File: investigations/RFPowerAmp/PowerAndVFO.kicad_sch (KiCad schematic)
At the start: 5 parts, among them J504 CONN_20

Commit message: Starting work on VFO
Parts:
- added Y601: ASTX-H11-25.000MHZ-T, ASTXH1124576MHZT, symbol ASTX-H11:ASTX-H11
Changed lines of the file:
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@@
     (effects (font (size 1.27 1.27)) (justify left top))
+  )
+  (symbol (lib_id "ASTX-H11:ASTX-H11") (at 39.37 43.18 0) (unit 1)
+    (in_bom yes) (on_board yes) (dnp no) (fields_autoplaced)
+    (property "Reference" "Y601" (at 59.69 35.56 0)
+      (effects (font (size 1.27 1.27)))
+    )
+    (property "Value" "ASTX-H11-25.000MHZ-T" (at 59.69 38.1 0)
+      (effects (font (size 1.27 1.27)))
+    )
+    (property "Footprint" "ASTXH1124576MHZT" (at 76.2 138.1 0)
+      (effects (font (size 1.27 1.27)) (justify left top) hide)
+    )
+    (property "Datasheet" "https://abracon.com/Oscillators/ASTX-H11.pdf" (at 76.2 238.1 0)
+      (effects (font (size 1.27 1.27)) (justify left top) hide)
+    )
+    (property "Height" "1.1" (at 76.2 438.1 0)
+      (effects (font (size 1.27 1.27)) (justify left top) hide)
+    )
+    (property "Manufacturer_Name" "ABRACON" (at 76.2 538.1 0)
+      (effects (font (size 1.27 1.27)) (justify left top) hide)
+    )
+    (property "Manufacturer_Part_Number" "ASTX-H11-##.###MHZ-T" (at 76.2 638.1 0)
+      (effects (font (size 1.27 1.27)) (justify left top) hide)
+    )
+    (property "Mouser Part Number" "815-ASTXH11" (at 76.2 738.1 0)
+      (effects (font (size 1.27 1.27)) (justify left top) hide)
+    )
+    (property "Mouser Price/Stock" "https://www.mouser.co.uk/ProductDetail/ABRACON/ASTX-H11-24000MHZ-T?qs=tfZGHB2PWd1qJqhLOR%252BN0w%3D%3D" (at 76.2 838.1 0)
+      (effects (font (size 1.27 1.27)) (justify left top) hide)
+    )
+    (property "Arrow Part Number" "ASTX-H11-##.###MHZ-T" (at 76.2 938.1 0)
+      (effects (font (size 1.27 1.27)) (justify left top) hide)
+    )
+    (property "Arrow Price/Stock" "https://www.arrow.com/en/products/astx-h11-24.000mhz-t/abracon" (at 76.2 1038.1 0)
+      (effects (font (size 1.27 1.27)) (justify left top) hide)
+    )
+    (pin "1")
+    (pin "2")
+    (pin "3")
+    (pin "4")
+    (instances
+      (project "RFPowerAmp"
+        (path "/4eeb911c-75f4-4119-b54f-fc9266b9abf0/204ca3ab-d207-410f-930a-76704dfa57fb"
+          (reference "Y601") (unit 1)
+        )
+      )
+    )
   )
   (symbol (lib_id "SparkFun-Connectors:CONN_20") (at 34.29 137.16 0) (mirror x) (unit 1)

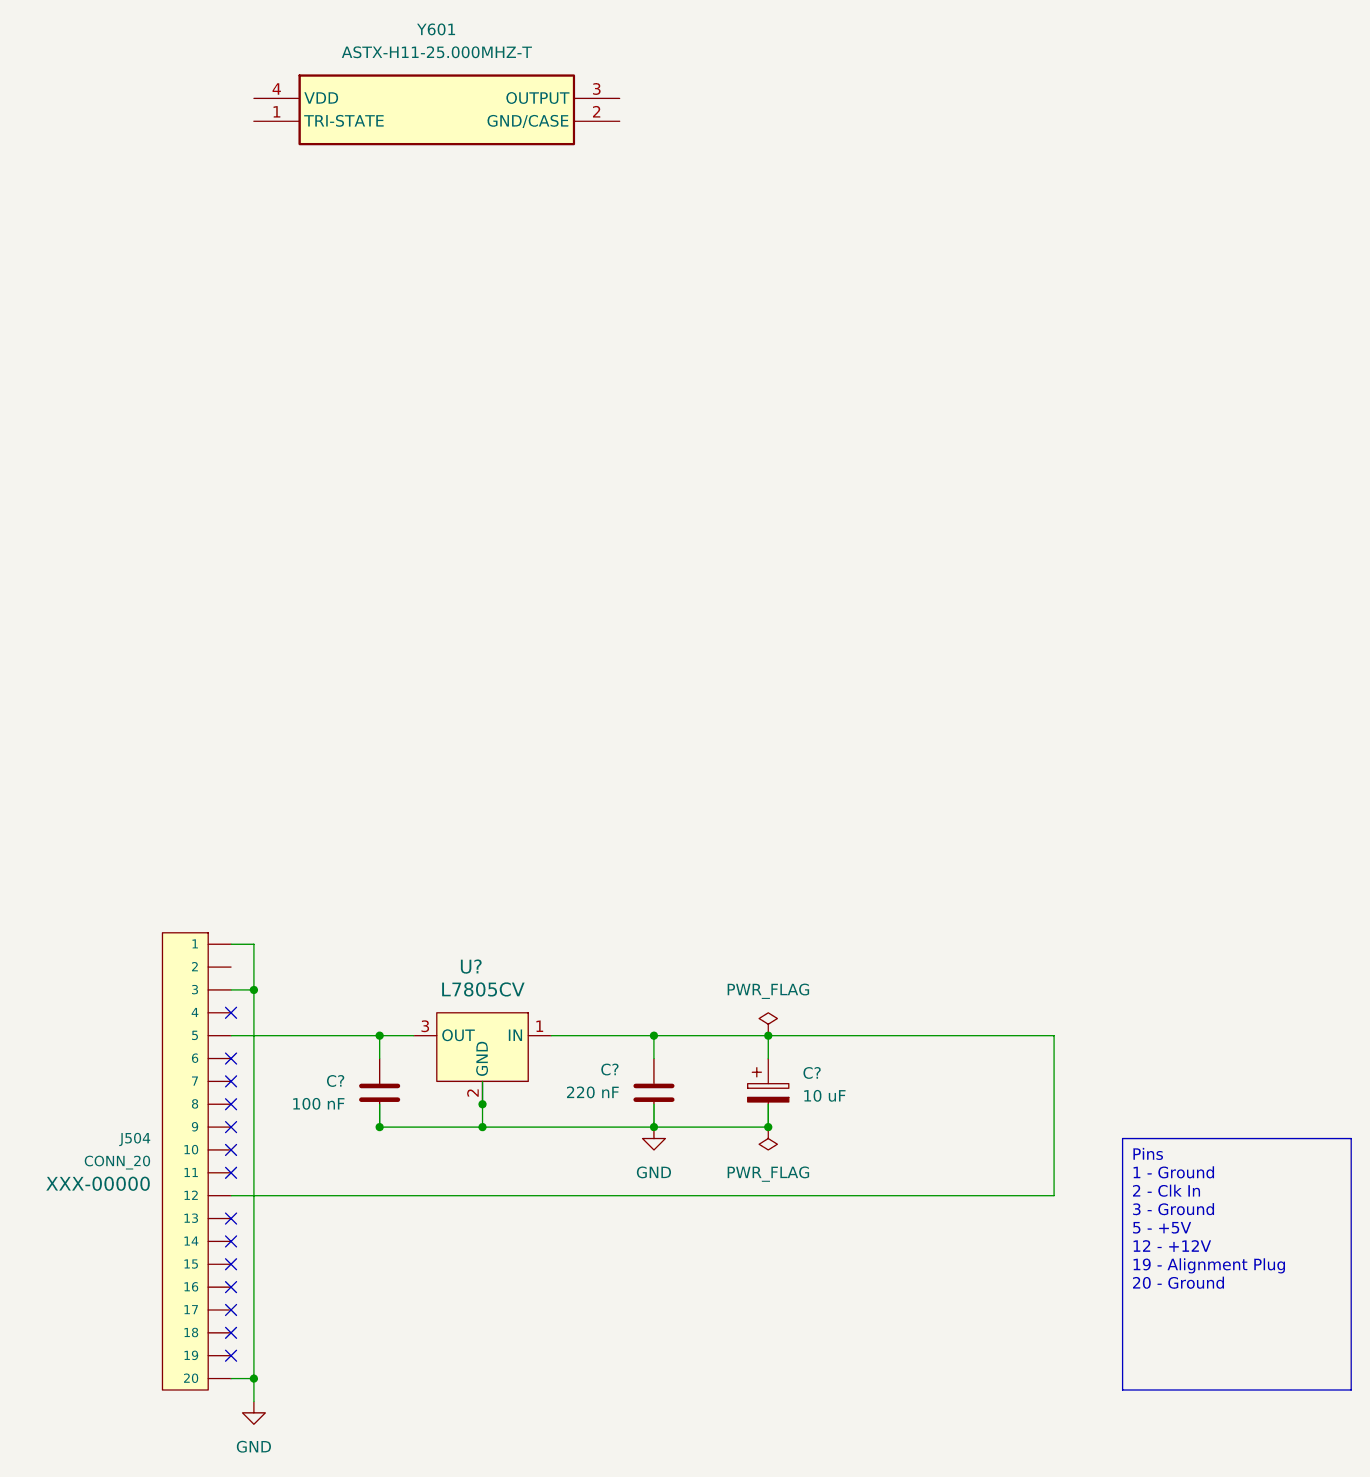
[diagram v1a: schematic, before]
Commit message: Updates .gitignore and investigations
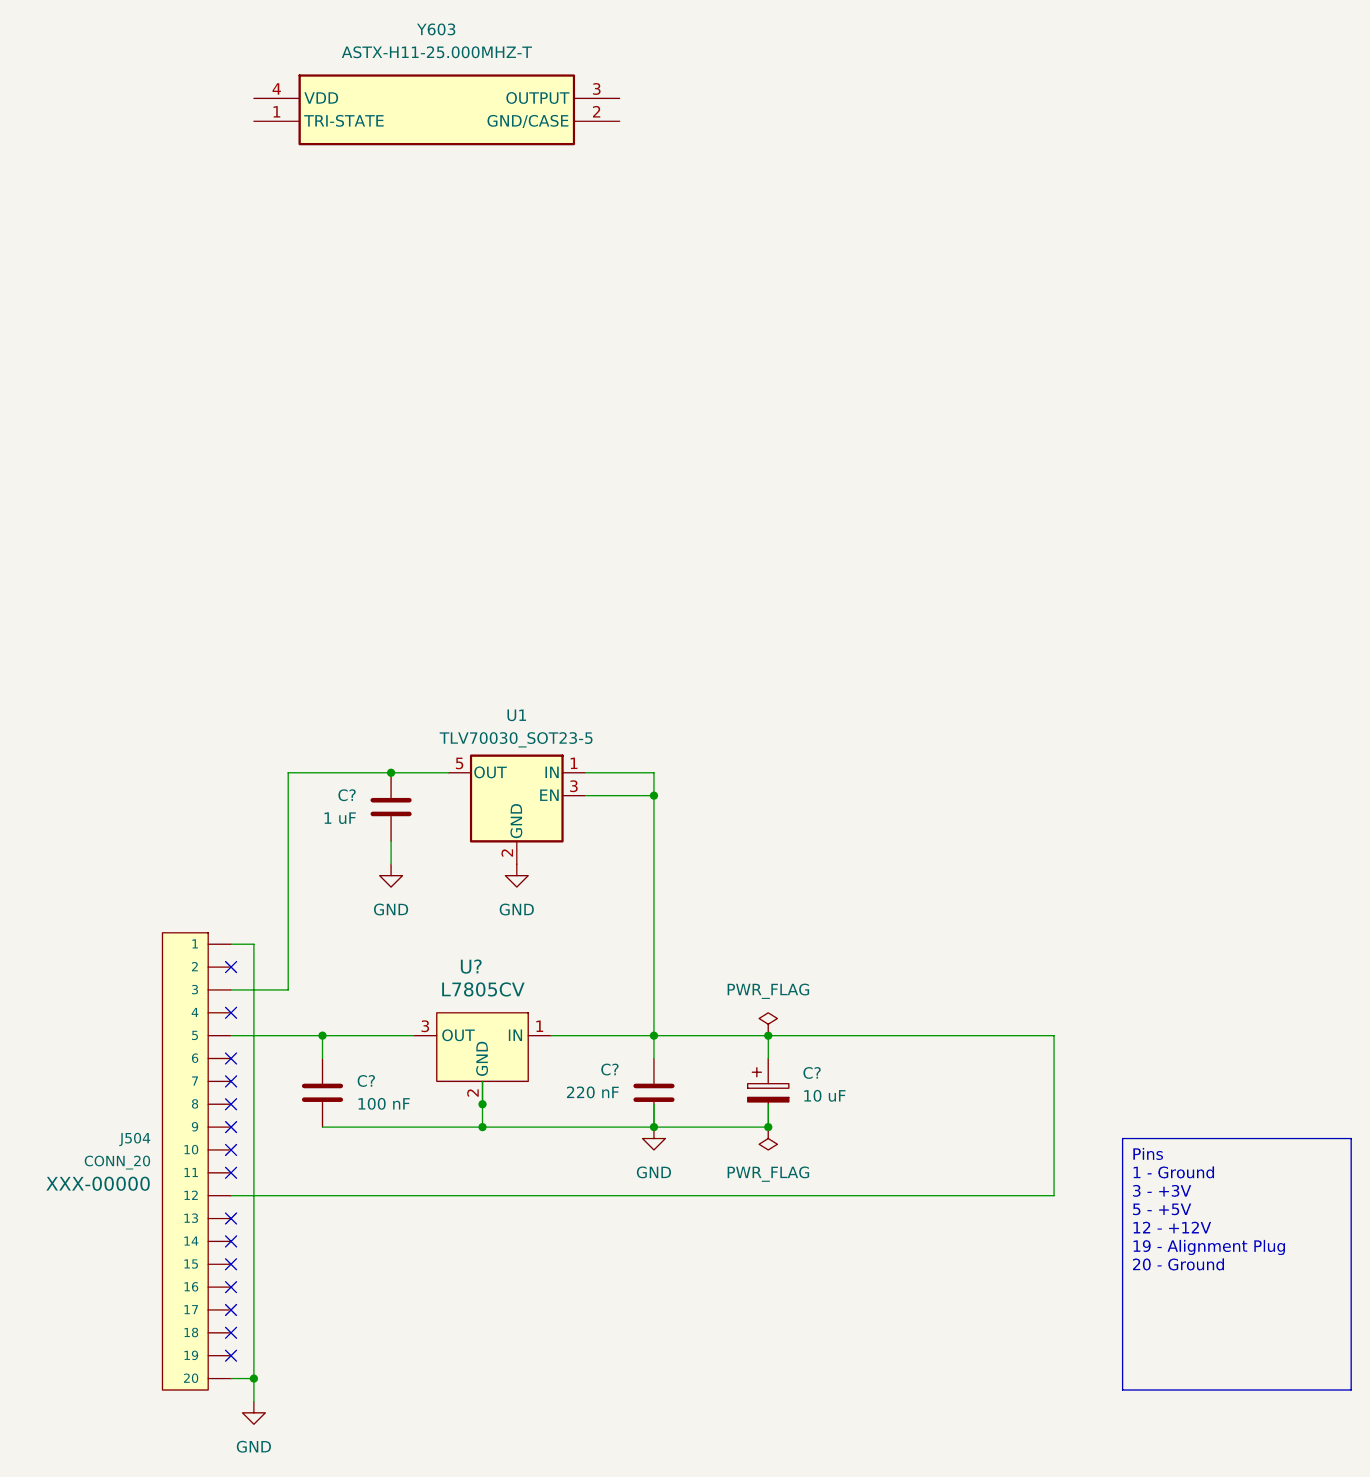
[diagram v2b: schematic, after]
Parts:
- added C?: 1 uF, Capacitor_SMD:C_0805_2012Metric, symbol Device:C
- added U1: TLV70030_SOT23-5, Package_TO_SOT_SMD:SOT-23-5, symbol Regulator_Linear:TLV70030_SOT23-5
- renumbered Y601 to Y603
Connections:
- net GND: now also C?.2, U1.2 (GND); no longer J504.3
- net at C?.1, C?.1, J504.12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: now also U1.1 (IN), U1.3 (EN)
- new net: C?.1, J504.3, U1.5 (OUT)
- no-connect marks 14 -> 15
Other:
- moved on the sheet: C?

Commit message: simulations
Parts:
- gave numbers to parts that had none: 5
- renumbered J504 to J1
